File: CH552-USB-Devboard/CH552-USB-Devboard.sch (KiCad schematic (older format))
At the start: 38 parts, among them J1 Conn_01x11_Male, J2 Conn_01x11_Male, J3 USB_C_Receptacle, J4 USB_C_Receptacle, SW1 SW_Push, SW2 SW_Push, U1 CH552T, U2 CH552G

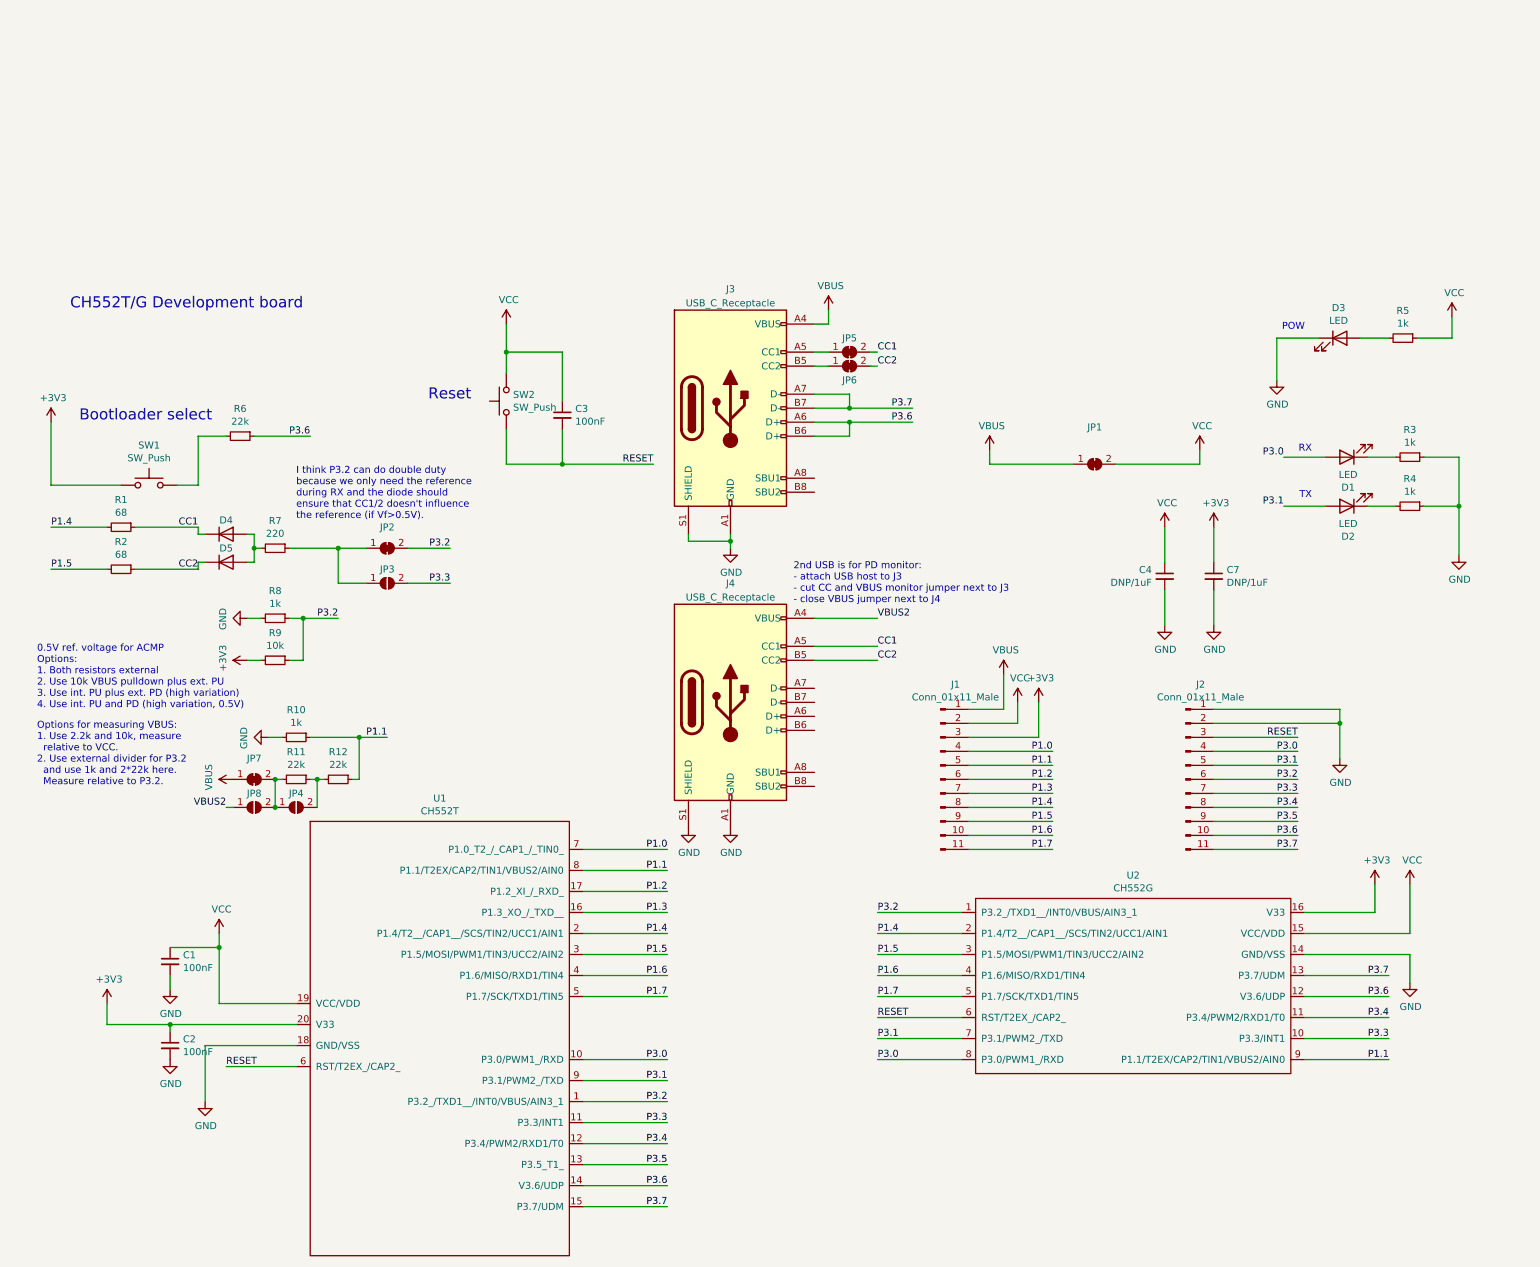
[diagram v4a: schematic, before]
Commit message: add LCSC part numbers
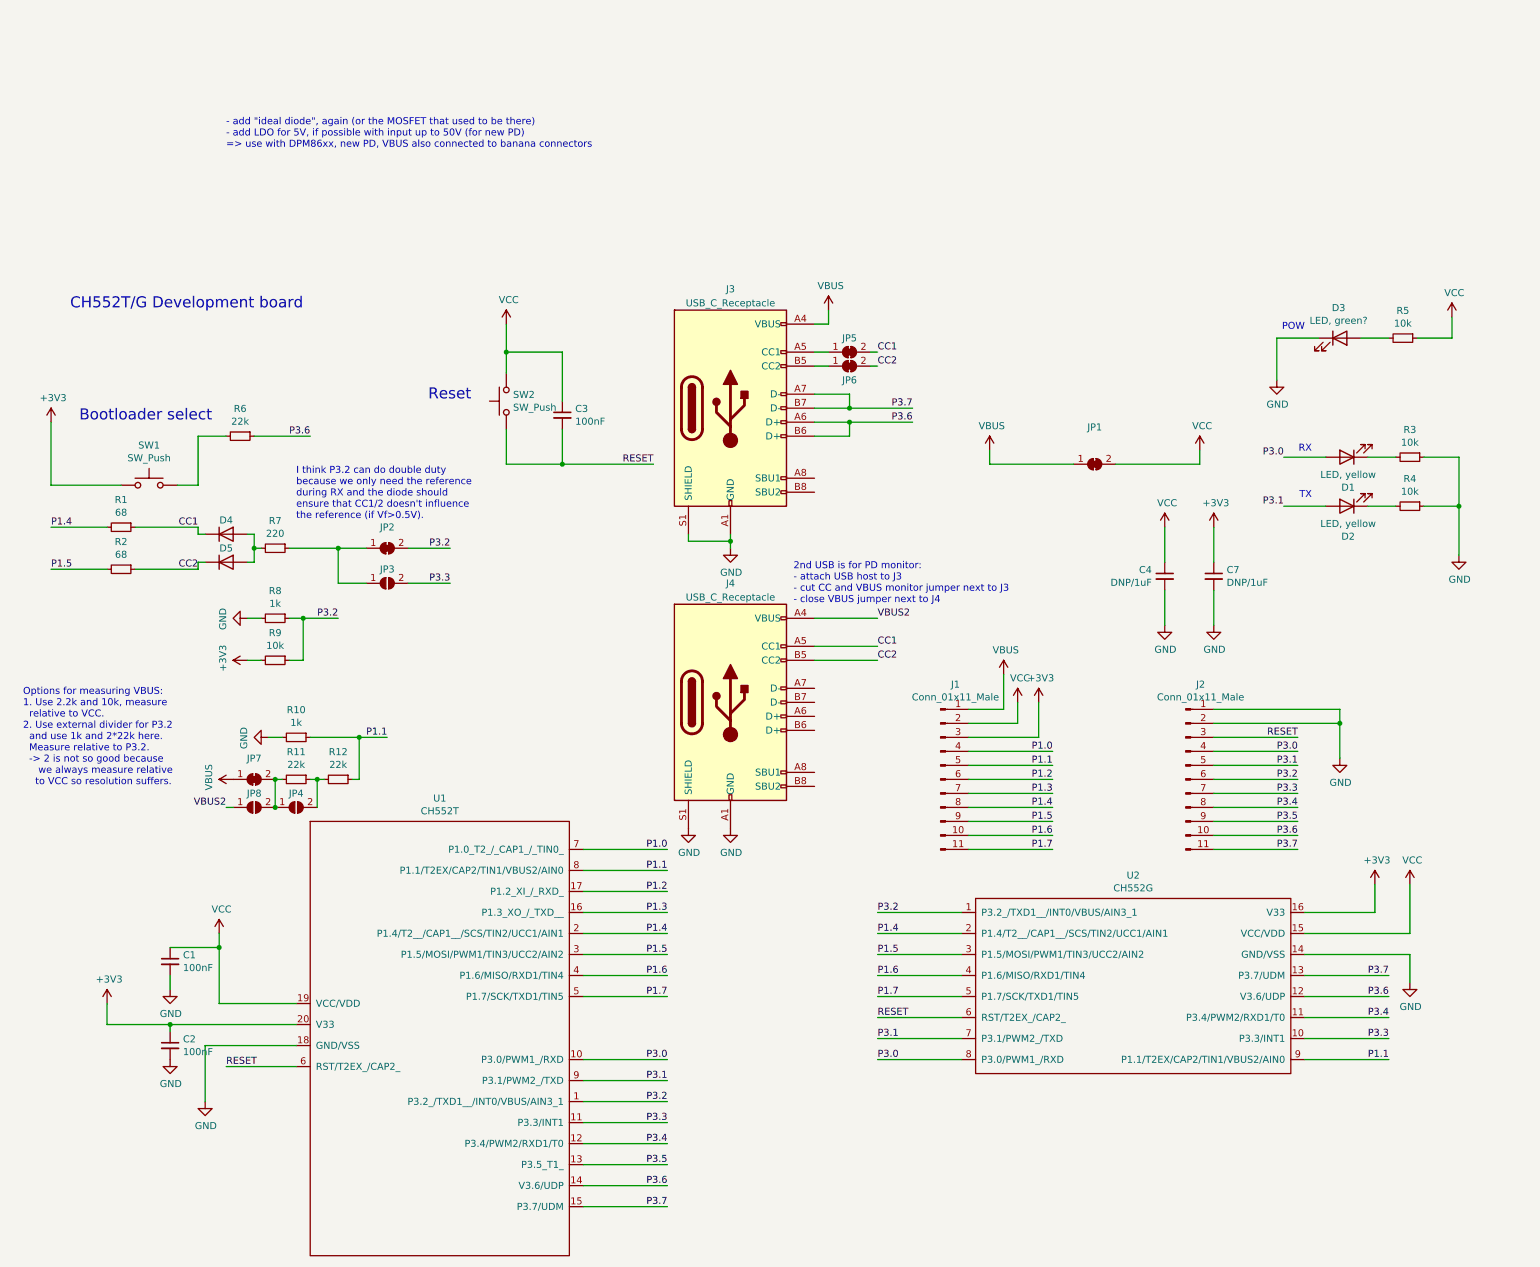
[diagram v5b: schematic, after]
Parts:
- C1, C2, C3: LCSC (none) -> C14663
- C4, C7: DNP (none) -> 1
- D1, D2: value LED -> LED, yellow; LCSC (none) -> C2296
- D3: value LED -> LED, green?; LCSC (none) -> C2297
- D4, D5: footprint Diode_SMD:D_SOD-523 -> Diode_SMD:D_SOD-323F; LCSC (none) -> C2128
- J1, J2: DNP (none) -> PCBA
- J3, J4: LCSC (none) -> C283540
- R1, R2: LCSC (none) -> C27592
- R10, R8: LCSC (none) -> C21190
- R11, R12, R6: LCSC (none) -> C31850
- R3, R4, R5: value 1k -> 10k; LCSC (none) -> C25804
- R7: LCSC (none) -> C22962
- R9: LCSC (none) -> C25804
- SW1, SW2: DNP (none) -> PCBA; LCSC (none) -> C116501
- U1: DNP (none) -> 1; LCSC (none) -> C111367
- U2: LCSC (none) -> C111292
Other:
- note added: "- add "ideal diode", again (or the MOSFET that used to be there)\n- add LDO for 5V, if possible with input up to 50V (for new PD)\n=> use with DPM86xx, new PD, VBUS also connected to banana connectors"
- note added: "Options for measuring VBUS:\n1. Use 2.2k and 10k, measure\n relative to VCC.\n2. Use external divider for P3.2\n and use 1k and 2*22k here.\n Measure relative to P3.2.\n -> 2 is not so good because\n we always measure relative\n to VCC so resolution suffers."
- note removed: "0.5V ref. voltage for ACMP\nOptions:\n1. Both resistors external\n2. Use 10k VBUS pulldown plus ext. PU\n3. Use int. PU plus ext. PD (high variation)\n4. Use int. PU and PD (high variation, 0.5V)"
- note removed: "Options for measuring VBUS:\n1. Use 2.2k and 10k, measure\n relative to VCC.\n2. Use external divider for P3.2\n and use 1k and 2*22k here.\n Measure relative to P3.2."
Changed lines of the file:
@@
 P 10500 1800
 F 0 "R3" V 10304 1800 50  0000 C CNN
-F 1 "1k" V 10395 1800 50  0000 C CNN
+F 1 "10k" V 10395 1800 50  0000 C CNN
 F 2 "Resistor_SMD:R_0603_1608Metric_Pad0.98x0.95mm_HandSolder" H 10500 1800 50  0001 C CNN
 F 3 "~" H 10500 1800 50  0001 C CNN
+F 4 "C25804" V 10500 1800 50  0001 C CNN "LCSC"
 	1    10500 1800
 	0    1    1    0
@@
 F 2 "Housings_SSOP:TSSOP-20_4.4x6.5mm_Pitch0.65mm" H 4100 5200 50  0001 C CNN
 F 3 "" H 4100 5200 50  0001 C CNN
+F 4 "C111367" H 3800 5200 50  0001 C CNN "LCSC"
+F 5 "1" H 3800 5200 50  0001 C CNN "DNP"
 	1    3800 5200
 	1    0    0    -1
@@
 F 2 "Housings_SOIC:SOIC-16_3.9x9.9mm_Pitch1.27mm" H 8850 5500 50  0001 C CNN
 F 3 "" H 8850 5500 50  0001 C CNN
+F 4 "C111292" H 8550 5500 50  0001 C CNN "LCSC"
 	1    8550 5500
 	1    0    0    -1
@@
 F 2 "Button_Switch_SMD:SW_SPST_PTS810" H 1500 2200 50  0001 C CNN
 F 3 "" H 1500 2200 50  0001 C CNN
+F 4 "C116501" H 1500 2000 50  0001 C CNN "LCSC"
+F 5 "PCBA" H 1500 2000 50  0001 C CNN "DNP"
 	1    1500 2000
 	1    0    0    -1
@@
 P 10050 1800
 F 0 "D1" H 10041 2016 50  0000 C CNN
-F 1 "LED" H 10041 1925 50  0000 C CNN
+F 1 "LED, yellow" H 10041 1925 50  0000 C CNN
 F 2 "LEDs:LED_0805" H 10050 1800 50  0001 C CNN
 F 3 "~" H 10050 1800 50  0001 C CNN
+F 4 "C2296" H 10050 1800 50  0001 C CNN "LCSC"
 	1    10050 1800
 	-1   0    0    1
@@
 P 10500 2150
 F 0 "R4" V 10304 2150 50  0000 C CNN
-F 1 "1k" V 10395 2150 50  0000 C CNN
+F 1 "10k" V 10395 2150 50  0000 C CNN
 F 2 "Resistor_SMD:R_0603_1608Metric_Pad0.98x0.95mm_HandSolder" H 10500 2150 50  0001 C CNN
 F 3 "~" H 10500 2150 50  0001 C CNN
+F 4 "C25804" V 10500 2150 50  0001 C CNN "LCSC"
 	1    10500 2150
 	0    1    1    0
@@
 P 10050 2150
 F 0 "D2" H 10041 2366 50  0000 C CNN
-F 1 "LED" H 10041 2275 50  0000 C CNN
+F 1 "LED, yellow" H 10041 2275 50  0000 C CNN
 F 2 "LEDs:LED_0805" H 10050 2150 50  0001 C CNN
 F 3 "~" H 10050 2150 50  0001 C CNN
+F 4 "C2296" H 10050 2150 50  0001 C CNN "LCSC"
 	1    10050 2150
 	-1   0    0    1
@@
 P 10450 950
 F 0 "R5" V 10254 950 50  0000 C CNN
-F 1 "1k" V 10345 950 50  0000 C CNN
+F 1 "10k" V 10345 950 50  0000 C CNN
 F 2 "Resistor_SMD:R_0603_1608Metric_Pad0.98x0.95mm_HandSolder" H 10450 950 50  0001 C CNN
 F 3 "~" H 10450 950 50  0001 C CNN
+F 4 "C25804" V 10450 950 50  0001 C CNN "LCSC"
 	1    10450 950
 	0    1    1    0
@@
 P 10000 950
 F 0 "D3" H 9991 1166 50  0000 C CNN
-F 1 "LED" H 9991 1075 50  0000 C CNN
+F 1 "LED, green?" H 9991 1075 50  0000 C CNN
 F 2 "LEDs:LED_0805" H 10000 950 50  0001 C CNN
 F 3 "~" H 10000 950 50  0001 C CNN
+F 4 "C2297" H 10000 950 50  0001 C CNN "LCSC"
 	1    10000 950
 	1    0    0    -1
@@
 F 2 "Capacitor_SMD:C_0603_1608Metric_Pad1.05x0.95mm_HandSolder" H 1650 5400 50  0001 C CNN
 F 3 "~" H 1650 5400 50  0001 C CNN
+F 4 "C14663" H 1650 5400 50  0001 C CNN "LCSC"
 	1    1650 5400
 	1    0    0    -1
@@
 F 2 "Capacitor_SMD:C_0603_1608Metric_Pad1.05x0.95mm_HandSolder" H 1650 6000 50  0001 C CNN
 F 3 "~" H 1650 6000 50  0001 C CNN
+F 4 "C14663" H 1650 6000 50  0001 C CNN "LCSC"
 	1    1650 6000
 	1    0    0    -1
@@
 F 2 "Capacitor_SMD:C_0603_1608Metric_Pad1.05x0.95mm_HandSolder" H 4450 1500 50  0001 C CNN
 F 3 "~" H 4450 1500 50  0001 C CNN
+F 4 "C14663" H 4450 1500 50  0001 C CNN "LCSC"
 	1    4450 1500
 	1    0    0    -1
@@
 F 2 "Button_Switch_SMD:SW_SPST_PTS810" H 4050 1600 50  0001 C CNN
 F 3 "" H 4050 1600 50  0001 C CNN
+F 4 "C116501" V 4050 1400 50  0001 C CNN "LCSC"
+F 5 "PCBA" V 4050 1400 50  0001 C CNN "DNP"
 	1    4050 1400
 	0    -1   -1   0
@@
 F 2 "Capacitor_SMD:C_0603_1608Metric_Pad1.05x0.95mm_HandSolder" H 8750 2650 50  0001 C CNN
 F 3 "~" H 8750 2650 50  0001 C CNN
+F 4 "1" H 8750 2650 50  0001 C CNN "DNP"
 	1    8750 2650
 	-1   0    0    -1
@@
 F 2 "Capacitor_SMD:C_0603_1608Metric_Pad1.05x0.95mm_HandSolder" H 9100 2650 50  0001 C CNN
 F 3 "~" H 9100 2650 50  0001 C CNN
+F 4 "1" H 9100 2650 50  0001 C CNN "DNP"
 	1    9100 2650
 	1    0    0    -1
@@
 F 2 "Connector_PinHeader_2.54mm:PinHeader_1x11_P2.54mm_Vertical" H 7150 4100 50  0001 C CNN
 F 3 "~" H 7150 4100 50  0001 C CNN
+F 4 "PCBA" H 7150 4100 50  0001 C CNN "DNP"
 	1    7150 4100
 	1    0    0    -1
@@
 F 2 "Connector_PinHeader_2.54mm:PinHeader_1x11_P2.54mm_Vertical" H 8900 4100 50  0001 C CNN
 F 3 "~" H 8900 4100 50  0001 C CNN
+F 4 "PCBA" H 8900 4100 50  0001 C CNN "DNP"
 	1    8900 4100
 	1    0    0    -1
@@
 F 2 "Resistor_SMD:R_0603_1608Metric_Pad0.98x0.95mm_HandSolder" H 2150 1650 50  0001 C CNN
 F 3 "~" H 2150 1650 50  0001 C CNN
+F 4 "C31850" V 2150 1650 50  0001 C CNN "LCSC"
 	1    2150 1650
 	0    1    1    0
@@
 F 2 "Resistor_SMD:R_0603_1608Metric_Pad0.98x0.95mm_HandSolder" H 1300 2300 50  0001 C CNN
 F 3 "~" H 1300 2300 50  0001 C CNN
+F 4 "C27592" V 1300 2300 50  0001 C CNN "LCSC"
 	1    1300 2300
 	0    1    1    0
@@
 F 2 "Resistor_SMD:R_0603_1608Metric_Pad0.98x0.95mm_HandSolder" H 1300 2600 50  0001 C CNN
 F 3 "~" H 1300 2600 50  0001 C CNN
+F 4 "C27592" V 1300 2600 50  0001 C CNN "LCSC"
 	1    1300 2600
 	0    1    1    0
@@
 F 0 "D4" H 2050 2450 50  0000 C CNN
 F 1 "e.g. 1N4148, C917006, C708767" H 2050 2476 50  0001 C CNN
-F 2 "Diode_SMD:D_SOD-523" H 2050 2350 50  0001 C CNN
+F 2 "Diode_SMD:D_SOD-323F" H 2050 2350 50  0001 C CNN
 F 3 "~" H 2050 2350 50  0001 C CNN
+F 4 "C2128" H 2050 2350 50  0001 C CNN "LCSC"
 	1    2050 2350
 	1    0    0    -1
@@
 F 2 "Resistor_SMD:R_0603_1608Metric_Pad0.98x0.95mm_HandSolder" H 2400 2450 50  0001 C CNN
 F 3 "~" H 2400 2450 50  0001 C CNN
+F 4 "C22962" V 2400 2450 50  0001 C CNN "LCSC"
 	1    2400 2450
 	0    1    1    0
@@
 F 0 "D5" H 2050 2650 50  0000 C CNN
 F 1 "e.g. 1N4148, C917006, C708767" H 2050 2676 50  0001 C CNN
-F 2 "Diode_SMD:D_SOD-523" H 2050 2550 50  0001 C CNN
+F 2 "Diode_SMD:D_SOD-323F" H 2050 2550 50  0001 C CNN
 F 3 "~" H 2050 2550 50  0001 C CNN
+F 4 "C2128" H 2050 2550 50  0001 C CNN "LCSC"
 	1    2050 2550
 	1    0    0    -1
@@
 F 2 "Resistor_SMD:R_0603_1608Metric_Pad0.98x0.95mm_HandSolder" H 2400 2950 50  0001 C CNN
 F 3 "~" H 2400 2950 50  0001 C CNN
+F 4 "C21190" V 2400 2950 50  0001 C CNN "LCSC"
 	1    2400 2950
 	0    1    1    0
@@
 F 2 "Resistor_SMD:R_0603_1608Metric_Pad0.98x0.95mm_HandSolder" H 2400 3250 50  0001 C CNN
 F 3 "~" H 2400 3250 50  0001 C CNN
+F 4 "C25804" V 2400 3250 50  0001 C CNN "LCSC"
 	1    2400 3250
 	0    1    1    0
@@
 Wire Wire Line
 	2200 2950 2300 2950
-Text Notes 700  3600 0    50   ~ 0
-0.5V ref. voltage for ACMP\nOptions:\n1. Both resistors external\n2. Use 10k VBUS pulldown plus ext. PU\n3. Use int. PU plus ext. PD (high variation)\n4. Use int. PU and PD (high variation, 0.5V)
 $Comp
 L Jumper:SolderJumper_2_Bridged JP2
@@
 F 2 "footprint:VACON_CSP_USC16_TR" H 5800 1450 50  0001 C CNN
 F 3 "http://www.usb.org/developers/docs/usb_31_033017.zip" H 5800 1450 50  0001 C CNN
+F 4 "C283540" H 5650 1450 50  0001 C CNN "LCSC"
 	1    5650 1450
 	1    0    0    -1
@@
 F 2 "Resistor_SMD:R_0603_1608Metric_Pad0.98x0.95mm_HandSolder" H 2550 3800 50  0001 C CNN
 F 3 "~" H 2550 3800 50  0001 C CNN
+F 4 "C21190" V 2550 3800 50  0001 C CNN "LCSC"
 	1    2550 3800
 	0    1    1    0
@@
 F 2 "Resistor_SMD:R_0603_1608Metric_Pad0.98x0.95mm_HandSolder" H 2550 4100 50  0001 C CNN
 F 3 "~" H 2550 4100 50  0001 C CNN
+F 4 "C31850" V 2550 4100 50  0001 C CNN "LCSC"
 	1    2550 4100
 	0    1    1    0
@@
 	3000 4100 3000 3800
 Connection ~ 3000 3800
-Text Notes 700  4150 0    50   ~ 0
-Options for measuring VBUS:\n1. Use 2.2k and 10k, measure\n  relative to VCC.\n2. Use external divider for P3.2\n  and use 1k and 2*22k here.\n  Measure relative to P3.2.
+Text Notes 600  4150 0    50   ~ 0
+Options for measuring VBUS:\n1. Use 2.2k and 10k, measure\n  relative to VCC.\n2. Use external divider for P3.2\n  and use 1k and 2*22k here.\n  Measure relative to P3.2.\n  -> 2 is not so good because\n     we always measure relative\n    to VCC so resolution suffers.
 $Comp
 L Device:R_Small R12
@@
 F 2 "Resistor_SMD:R_0603_1608Metric_Pad0.98x0.95mm_HandSolder" H 2850 4100 50  0001 C CNN
 F 3 "~" H 2850 4100 50  0001 C CNN
+F 4 "C31850" V 2850 4100 50  0001 C CNN "LCSC"
 	1    2850 4100
 	0    1    1    0
@@
 F 2 "footprint:VACON_CSP_USC16_TR" H 5800 3550 50  0001 C CNN
 F 3 "http://www.usb.org/developers/docs/usb_31_033017.zip" H 5800 3550 50  0001 C CNN
+F 4 "C283540" H 5650 3550 50  0001 C CNN "LCSC"
 	1    5650 3550
 	1    0    0    -1
@@
 Connection ~ 2400 4300
 Connection ~ 2400 4100
+Text Notes 2050 -400 0    50   ~ 0
+- add "ideal diode", again (or the MOSFET that used to be there)\n- add LDO for 5V, if possible with input up to 50V (for new PD)\n=> use with DPM86xx, new PD, VBUS also connected to banana connectors
 $EndSCHEMATC
